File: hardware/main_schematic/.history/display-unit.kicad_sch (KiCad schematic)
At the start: 1 part, among them U5 STM32L476RGTx

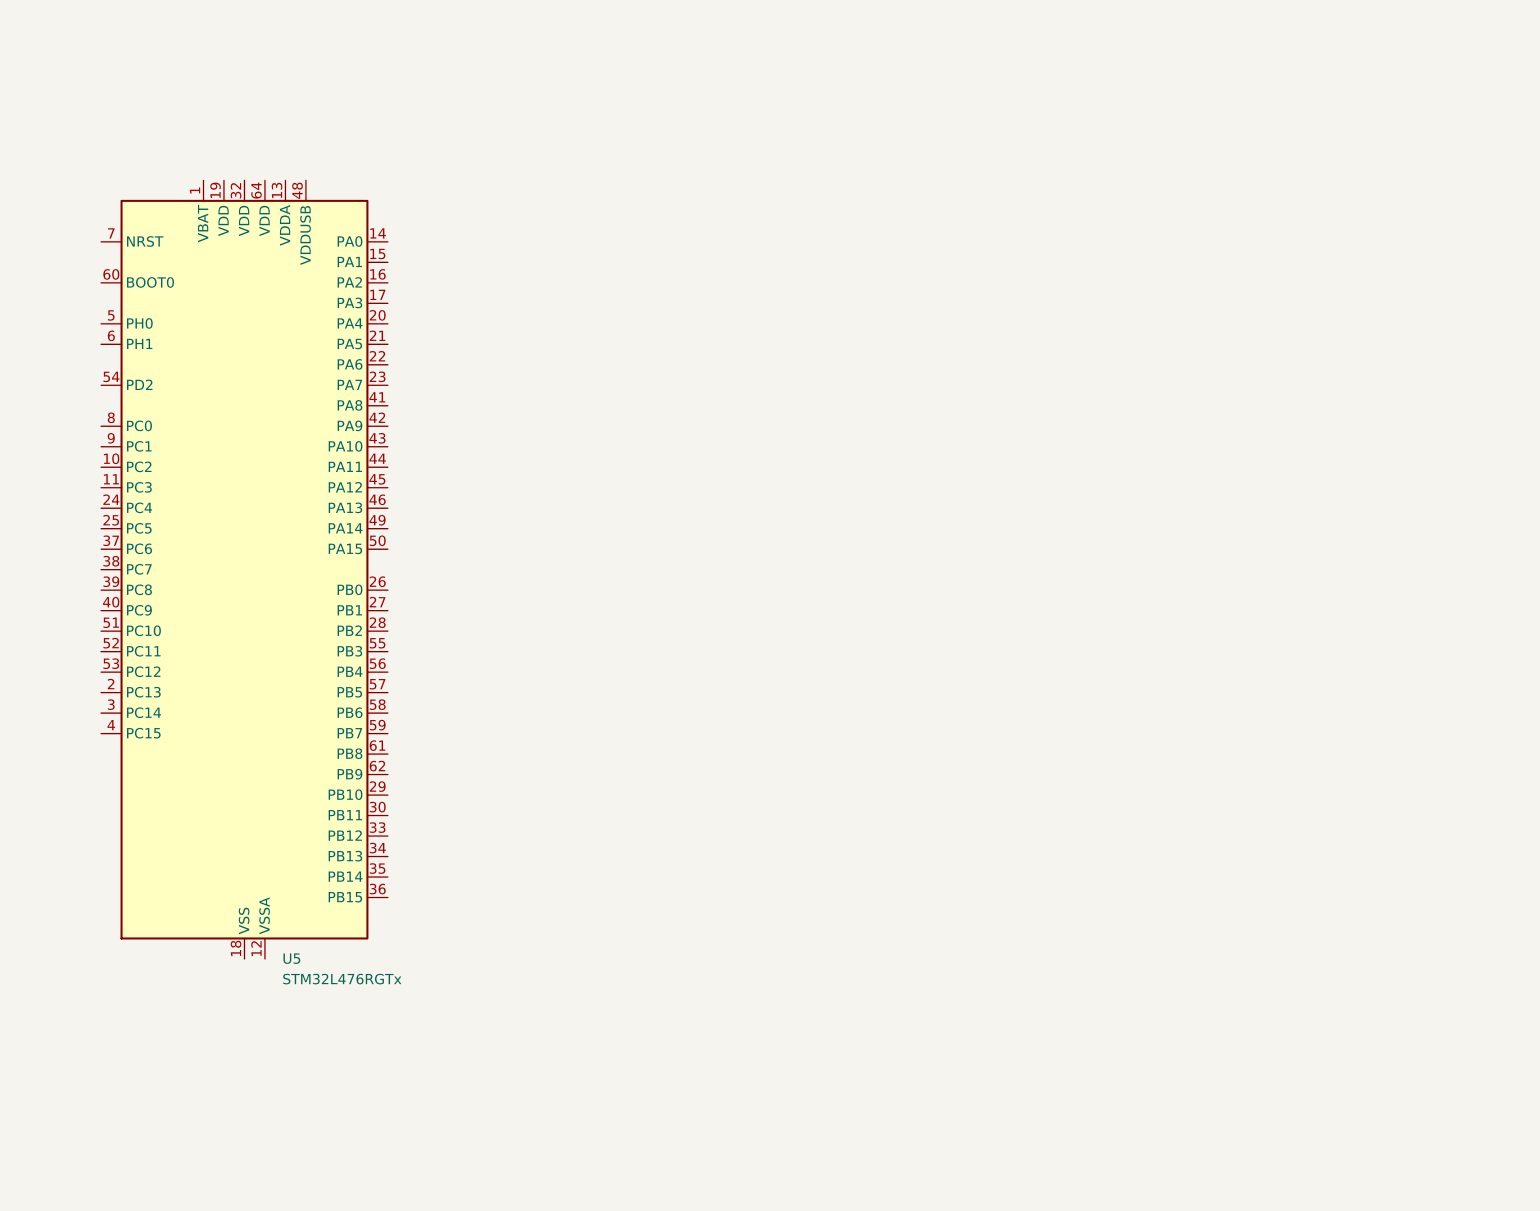
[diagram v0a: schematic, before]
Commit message: Schematic done
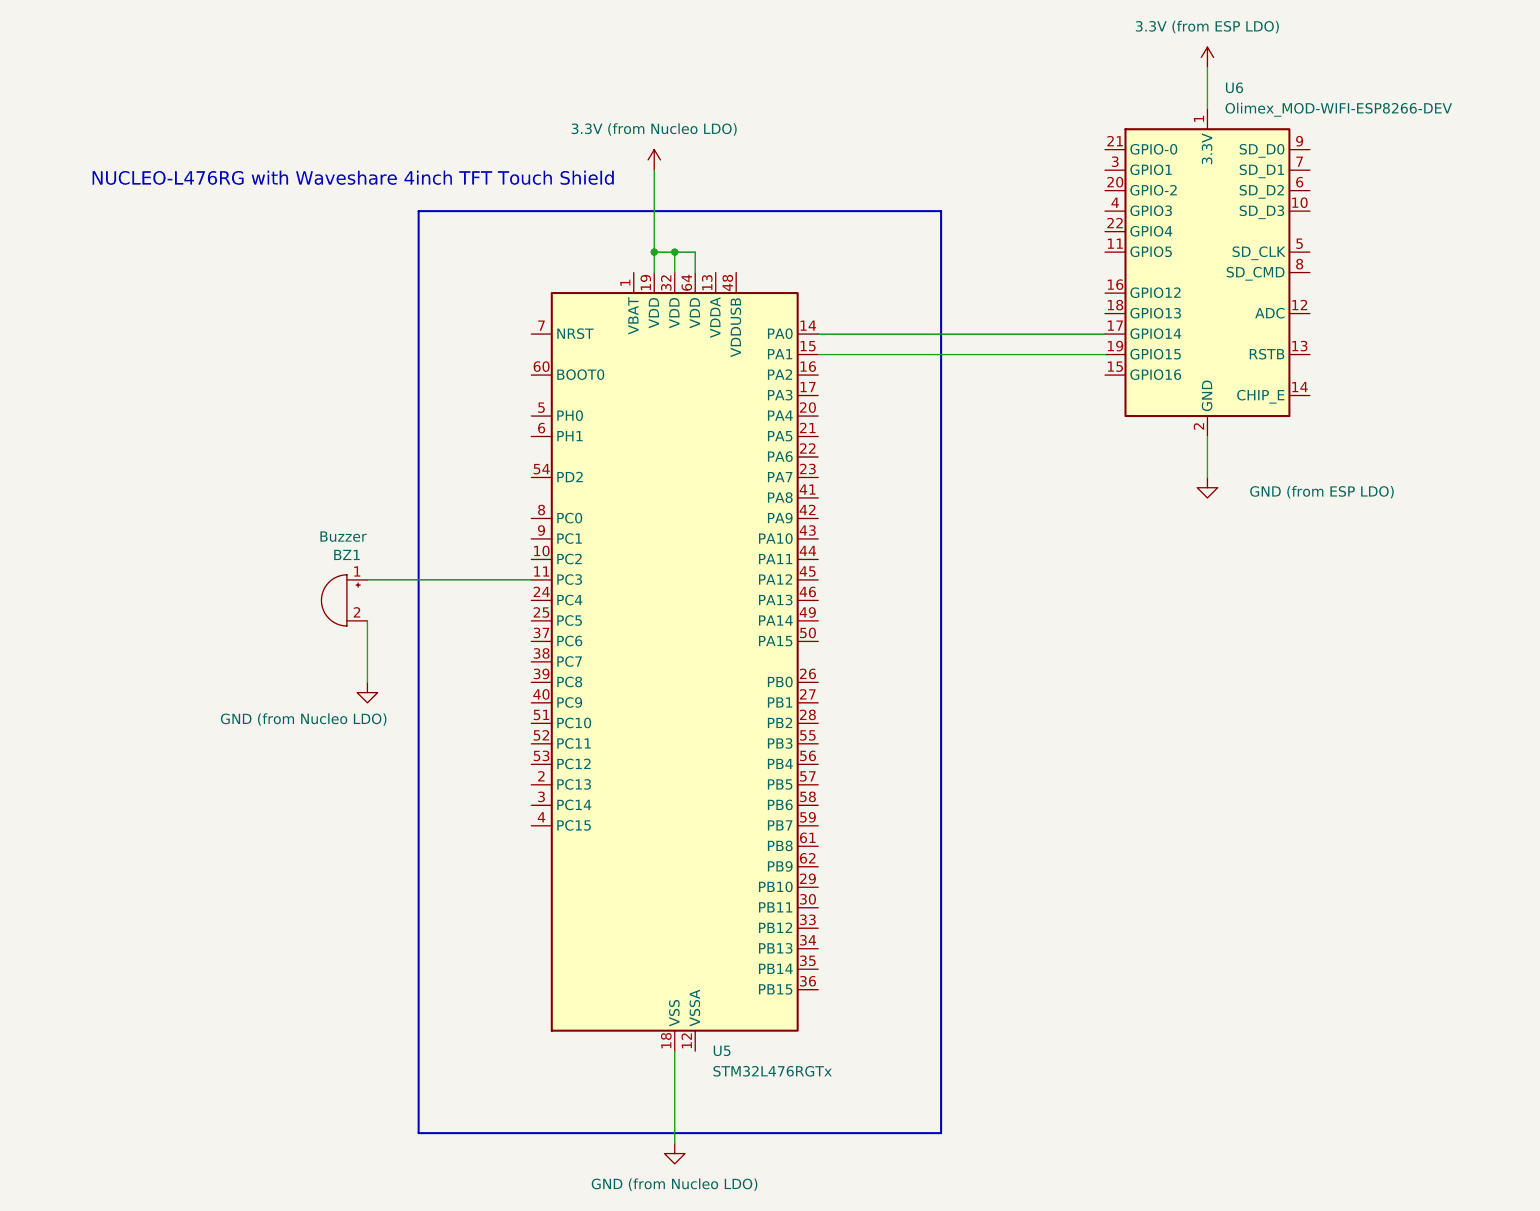
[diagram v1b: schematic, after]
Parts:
- added BZ1: Buzzer, symbol Device:Buzzer
- added U6: Olimex_MOD-WIFI-ESP8266-DEV, Module:Olimex_MOD-WIFI-ESP8266-DEV, symbol MCU_Module:Olimex_MOD-WIFI-ESP8266-DEV
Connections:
- net at U5.11 (PC3): now also BZ1.1 (+)
- net at U5.14 (PA0): now also U6.17 (GPIO14)
- net at U5.15 (PA1): now also U6.19 (GPIO15)
- net GND (from Nucleo LDO): now reaches U5.18 (VSS), U5.31 (VSS), U5.47 (VSS), U5.63 (VSS)
- net GND (from Nucleo LDO): now also BZ1.2 (-)
- net 3.3V (from Nucleo LDO): now reaches U5.19 (VDD)
- net 3.3V (from Nucleo LDO): now also U5.32 (VDD), U5.64 (VDD)
- new net 3.3V (from ESP LDO): U6.1 (3.3V)
- new net GND (from ESP LDO): U6.2 (GND)
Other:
- note added: "NUCLEO-L476RG with Waveshare 4inch TFT Touch Shield"
- moved on the sheet: U5
